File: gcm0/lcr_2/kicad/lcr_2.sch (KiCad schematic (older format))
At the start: 131 parts, among them J1 5V, J2 -5V, J3 Conn_01x01_Male, J4 Conn_01x03_Male, J5 Conn_01x01_Male, J6 Conn_01x01_Male, J8 SWD, Q1 BC547, Q2 BC547, Q3 BC547, SW1 1, SW2 2, U1 RC4580, U10 RC4580, U11 74HC595, U12 STM32F030F4P6, U2 74HC4053PW,112, U3 74HC4052PW,118, U4 RC4580, U5 LM2596S-5, U6 LM7805_TO220, U7 RC4580, U8 LM1117-3.3, U9 74HC4053PW,112, Y1 8M

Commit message: 相位幅度校准程序成功
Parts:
- added R21: 100, Resistor_THT:R_Axial_DIN0204_L3.6mm_D1.6mm_P1.90mm_Vertical, symbol Device:R
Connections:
- net GND: now also R21.2
- net at C16.1, C2.1, R19.1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: now also R21.1
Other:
- moved on the sheet: R22
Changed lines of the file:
@@
 	3500 2750 4450 2750
 Connection ~ 4450 2750
-Text Label 5600 1550 0    50   ~ 0
+Text Label 6200 1100 0    50   ~ 0
 SPWM
 $Comp
@@
 L Device:R R22
 U 1 1 625D8345
-P 5300 1550
-F 0 "R22" V 5093 1550 50  0000 C CNN
-F 1 "1K" V 5184 1550 50  0000 C CNN
-F 2 "Resistor_THT:R_Axial_DIN0204_L3.6mm_D1.6mm_P1.90mm_Vertical" V 5230 1550 50  0001 C CNN
-F 3 "~" H 5300 1550 50  0001 C CNN
-	1    5300 1550
-	0    1    1    0
-$EndComp
-Wire Wire Line
-	5150 1550 5000 1550
+P 5900 1100
+F 0 "R22" V 5693 1100 50  0000 C CNN
+F 1 "1K" V 5784 1100 50  0000 C CNN
+F 2 "Resistor_THT:R_Axial_DIN0204_L3.6mm_D1.6mm_P1.90mm_Vertical" V 5830 1100 50  0001 C CNN
+F 3 "~" H 5900 1100 50  0001 C CNN
+	1    5900 1100
+	0    1    1    0
+$EndComp
 Connection ~ 5000 1550
 Wire Wire Line
-	5450 1550 5600 1550
+	6050 1100 6200 1100
 Wire Wire Line
 	3700 1550 4100 1550
@@
 	0    1    1    0
 $EndComp
+Wire Wire Line
+	5750 1100 5350 1100
+Wire Wire Line
+	5000 1100 5000 1550
+$Comp
+L Device:R R21
+U 1 1 61E47858
+P 5350 1250
+F 0 "R21" H 5420 1296 50  0000 L CNN
+F 1 "100" H 5420 1205 50  0000 L CNN
+F 2 "Resistor_THT:R_Axial_DIN0204_L3.6mm_D1.6mm_P1.90mm_Vertical" V 5280 1250 50  0001 C CNN
+F 3 "~" H 5350 1250 50  0001 C CNN
+	1    5350 1250
+	1    0    0    -1
+$EndComp
+Connection ~ 5350 1100
+Wire Wire Line
+	5350 1100 5000 1100
+$Comp
+L power:GND #PWR09
+U 1 1 61F0040F
+P 5350 1400
+F 0 "#PWR09" H 5350 1150 50  0001 C CNN
+F 1 "GND" H 5355 1227 50  0000 C CNN
+F 2 "" H 5350 1400 50  0001 C CNN
+F 3 "" H 5350 1400 50  0001 C CNN
+	1    5350 1400
+	1    0    0    -1
+$EndComp
 $EndSCHEMATC

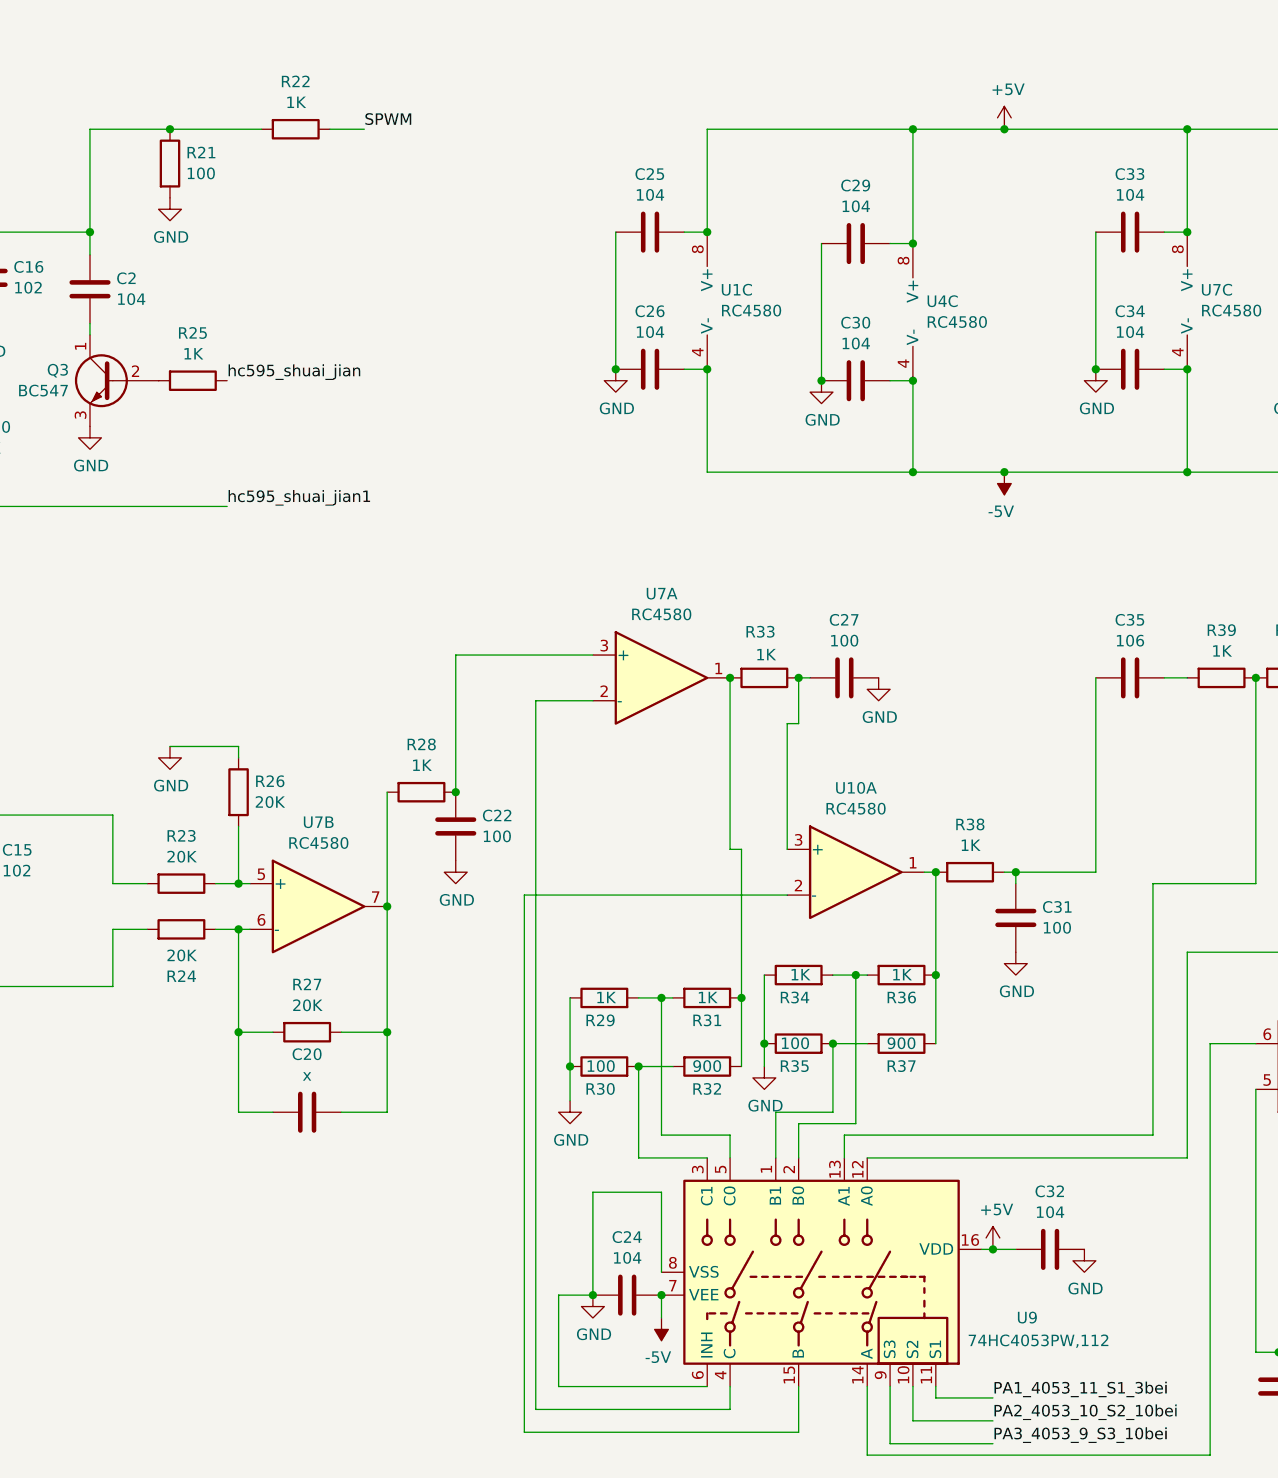
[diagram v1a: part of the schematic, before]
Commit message: 修改100KHZ的ADC触发方式
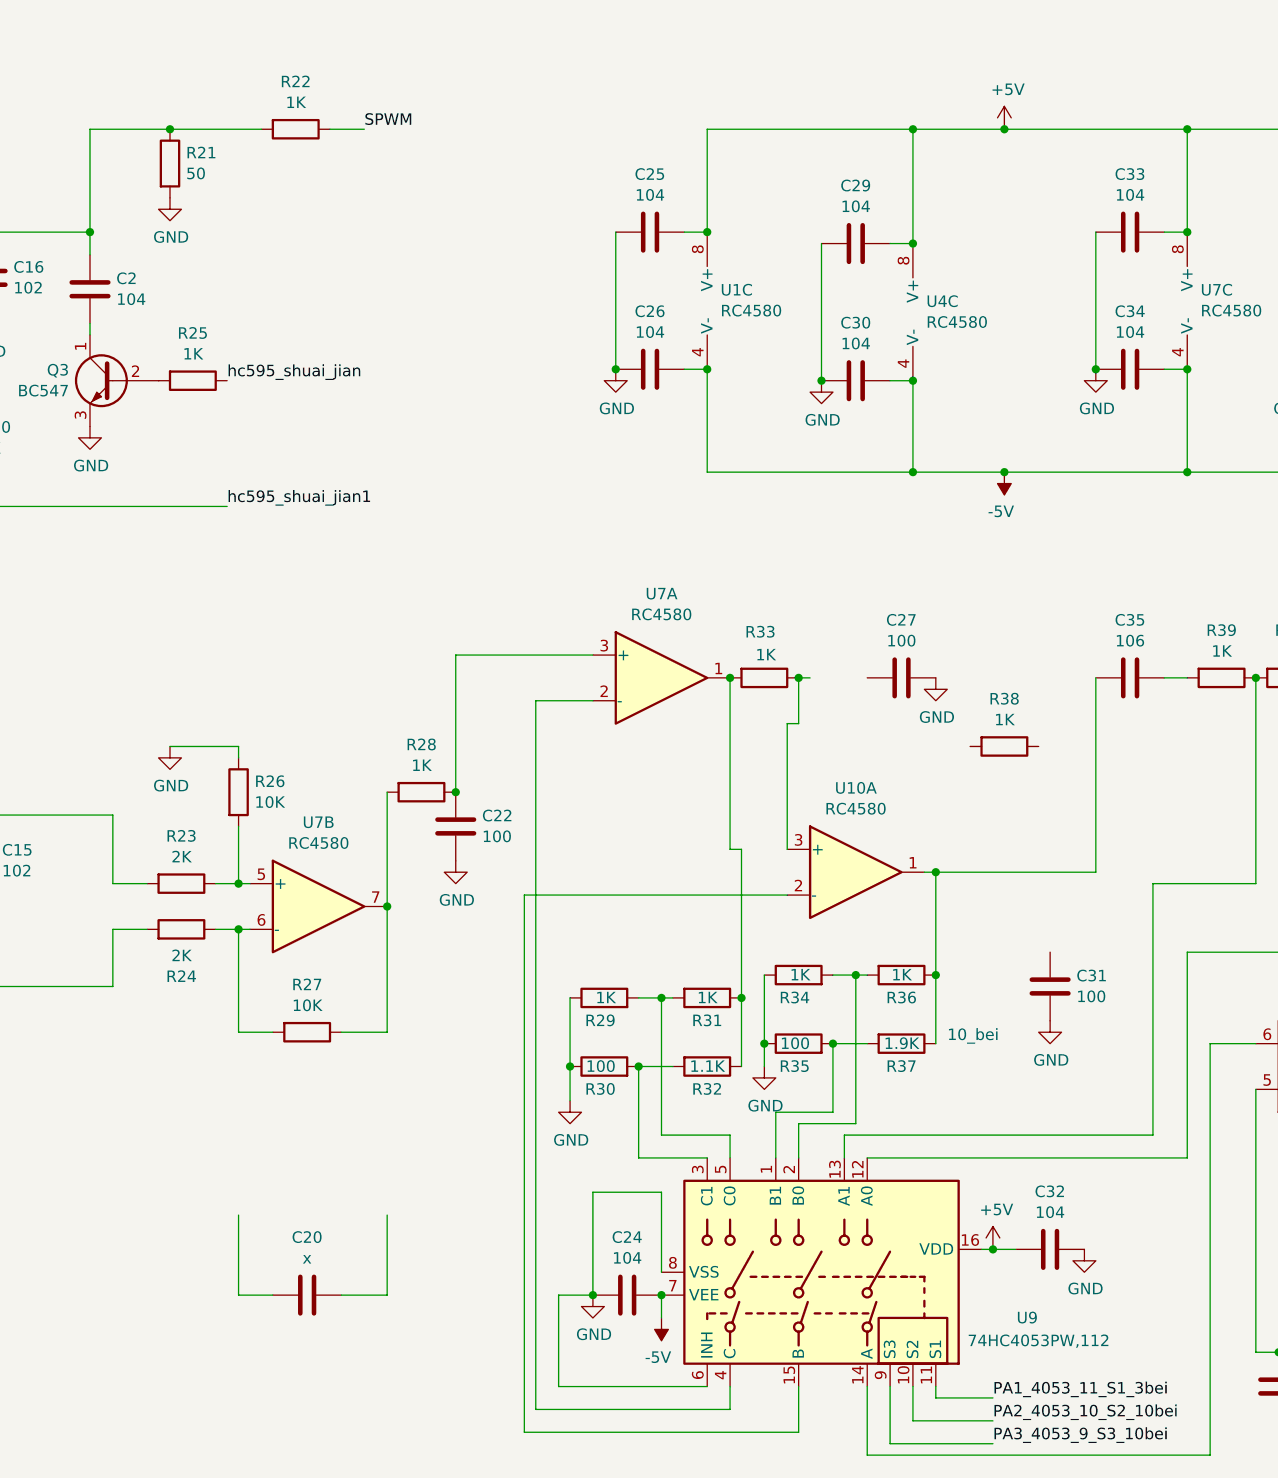
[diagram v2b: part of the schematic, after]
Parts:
- R21: value 100 -> 50
- R23, R24: value 20K -> 2K
- R26, R27: value 20K -> 10K
- R32: value 900 -> 1.1K
- R37: value 900 -> 1.9K
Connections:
- net at R24.1, R27.2, U7.6 (-): no longer C20.2
- net at R27.1, R28.2, U7.7: no longer C20.1
- net at R33.1, U10.3 (+): no longer C27.2
- net at R36.1, R37.1, U10.1: now also C35.2; no longer R38.2
- now unconnected: C31.1, R38.1
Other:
- note added: "10_bei"
- moved on the sheet: C20, C27, C31, R38
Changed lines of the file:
@@
 P 5400 4400
 F 0 "R23" V 5193 4400 50  0000 C CNN
-F 1 "20K" V 5284 4400 50  0000 C CNN
+F 1 "2K" V 5284 4400 50  0000 C CNN
 F 2 "Resistor_THT:R_Axial_DIN0204_L3.6mm_D1.6mm_P1.90mm_Vertical" V 5330 4400 50  0001 C CNN
 F 3 "~" H 5400 4400 50  0001 C CNN
@@
 P 5400 4600
 F 0 "R24" V 5193 4600 50  0000 C CNN
-F 1 "20K" V 5284 4600 50  0000 C CNN
+F 1 "2K" V 5284 4600 50  0000 C CNN
 F 2 "Resistor_THT:R_Axial_DIN0204_L3.6mm_D1.6mm_P1.90mm_Vertical" V 5330 4600 50  0001 C CNN
 F 3 "~" H 5400 4600 50  0001 C CNN
@@
 P 5650 4000
 F 0 "R26" H 5720 4046 50  0000 L CNN
-F 1 "20K" H 5720 3955 50  0000 L CNN
+F 1 "10K" H 5720 3955 50  0000 L CNN
 F 2 "Resistor_THT:R_Axial_DIN0204_L3.6mm_D1.6mm_P1.90mm_Vertical" V 5580 4000 50  0001 C CNN
 F 3 "~" H 5650 4000 50  0001 C CNN
@@
 P 5950 5050
 F 0 "R27" V 5743 5050 50  0000 C CNN
-F 1 "20K" V 5834 5050 50  0000 C CNN
+F 1 "10K" V 5834 5050 50  0000 C CNN
 F 2 "Resistor_THT:R_Axial_DIN0204_L3.6mm_D1.6mm_P1.90mm_Vertical" V 5880 5050 50  0001 C CNN
 F 3 "~" H 5950 5050 50  0001 C CNN
@@
 P 8550 5100
 F 0 "R37" V 8650 5100 50  0000 C CNN
-F 1 "900" V 8550 5100 50  0000 C CNN
+F 1 "1.9K" V 8550 5100 50  0000 C CNN
 F 2 "Resistor_THT:R_Axial_DIN0204_L3.6mm_D1.6mm_P1.90mm_Vertical" V 8480 5100 50  0001 C CNN
 F 3 "~" H 8550 5100 50  0001 C CNN
@@
 	0    1    1    0
 $EndComp
-$Comp
-L Device:C C22
-U 1 1 631C5B0A
-P 6600 4150
-F 0 "C22" H 6715 4196 50  0000 L CNN
-F 1 "100" H 6715 4105 50  0000 L CNN
-F 2 "Capacitor_SMD:C_0603_1608Metric_Pad1.08x0.95mm_HandSolder" H 6638 4000 50  0001 C CNN
-F 3 "~" H 6600 4150 50  0001 C CNN
-	1    6600 4150
-	1    0    0    -1
-$EndComp
-$Comp
-L power:GND #PWR035
-U 1 1 631C7937
-P 6600 4300
-F 0 "#PWR035" H 6600 4050 50  0001 C CNN
-F 1 "GND" H 6605 4127 50  0000 C CNN
-F 2 "" H 6600 4300 50  0001 C CNN
-F 3 "" H 6600 4300 50  0001 C CNN
-	1    6600 4300
-	1    0    0    -1
-$EndComp
 Wire Wire Line
 	7200 3400 6600 3400
@@
 Wire Wire Line
 	6600 3400 6600 4000
-Connection ~ 6600 4000
 $Comp
 L Device:C C27
 U 1 1 632A707B
-P 8300 3500
-F 0 "C27" V 8048 3500 50  0000 C CNN
-F 1 "100" V 8139 3500 50  0000 C CNN
-F 2 "Capacitor_SMD:C_0603_1608Metric_Pad1.08x0.95mm_HandSolder" H 8338 3350 50  0001 C CNN
-F 3 "~" H 8300 3500 50  0001 C CNN
-	1    8300 3500
+P 8550 3500
+F 0 "C27" V 8298 3500 50  0000 C CNN
+F 1 "100" V 8389 3500 50  0000 C CNN
+F 2 "Capacitor_SMD:C_0603_1608Metric_Pad1.08x0.95mm_HandSolder" H 8588 3350 50  0001 C CNN
+F 3 "~" H 8550 3500 50  0001 C CNN
+	1    8550 3500
 	0    1    1    0
 $EndComp
@@
 L power:GND #PWR039
 U 1 1 632AA5CA
-P 8450 3500
-F 0 "#PWR039" H 8450 3250 50  0001 C CNN
-F 1 "GND" H 8455 3327 50  0000 C CNN
-F 2 "" H 8450 3500 50  0001 C CNN
-F 3 "" H 8450 3500 50  0001 C CNN
-	1    8450 3500
+P 8700 3500
+F 0 "#PWR039" H 8700 3250 50  0001 C CNN
+F 1 "GND" H 8705 3327 50  0000 C CNN
+F 2 "" H 8700 3500 50  0001 C CNN
+F 3 "" H 8700 3500 50  0001 C CNN
+	1    8700 3500
 	1    0    0    -1
 $EndComp
@@
 Wire Wire Line
 	10100 3500 10100 4400
-$Comp
-L Device:R R38
-U 1 1 63573DB8
-P 8850 4350
-F 0 "R38" V 8643 4350 50  0000 C CNN
-F 1 "1K" V 8734 4350 50  0000 C CNN
-F 2 "Resistor_THT:R_Axial_DIN0204_L3.6mm_D1.6mm_P1.90mm_Vertical" V 8780 4350 50  0001 C CNN
-F 3 "~" H 8850 4350 50  0001 C CNN
-	1    8850 4350
-	0    1    1    0
-$EndComp
-$Comp
-L Device:C C31
-U 1 1 63575BE7
-P 9050 4550
-F 0 "C31" H 9165 4596 50  0000 L CNN
-F 1 "100" H 9165 4505 50  0000 L CNN
-F 2 "Capacitor_SMD:C_0603_1608Metric_Pad1.08x0.95mm_HandSolder" H 9088 4400 50  0001 C CNN
-F 3 "~" H 9050 4550 50  0001 C CNN
-	1    9050 4550
-	1    0    0    -1
-$EndComp
-$Comp
-L power:GND #PWR049
-U 1 1 6357784C
-P 9050 4700
-F 0 "#PWR049" H 9050 4450 50  0001 C CNN
-F 1 "GND" H 9055 4527 50  0000 C CNN
-F 2 "" H 9050 4700 50  0001 C CNN
-F 3 "" H 9050 4700 50  0001 C CNN
-	1    9050 4700
-	1    0    0    -1
-$EndComp
-Wire Wire Line
-	9000 4350 9050 4350
 Wire Wire Line
 	9400 4350 9400 3500
-Wire Wire Line
-	9050 4400 9050 4350
-Connection ~ 9050 4350
-Wire Wire Line
-	9050 4350 9400 4350
 $Comp
 L Switch:SW_Push SW1
@@
 Wire Wire Line
 	8700 4800 8700 4350
-Connection ~ 8700 4350
 Wire Wire Line
 	8700 5100 8700 4800
@@
 P 7700 5200
 F 0 "R32" V 7800 5200 50  0000 C CNN
-F 1 "900" V 7700 5200 50  0000 C CNN
+F 1 "1.1K" V 7700 5200 50  0000 C CNN
 F 2 "Resistor_THT:R_Axial_DIN0204_L3.6mm_D1.6mm_P1.90mm_Vertical" V 7630 5200 50  0001 C CNN
 F 3 "~" H 7700 5200 50  0001 C CNN
@@
 	0    1    1    0
 $EndComp
-Connection ~ 5650 5050
-Wire Wire Line
-	5650 5400 5650 5050
-Wire Wire Line
-	5800 5400 5650 5400
-Connection ~ 6300 5050
-Wire Wire Line
-	6300 5400 6300 5050
-Wire Wire Line
-	6100 5400 6300 5400
-$Comp
-L Device:C C20
-U 1 1 620378E4
-P 5950 5400
-F 0 "C20" V 5698 5400 50  0000 C CNN
-F 1 "x" V 5789 5400 50  0000 C CNN
-F 2 "Capacitor_SMD:C_0603_1608Metric_Pad1.08x0.95mm_HandSolder" H 5988 5250 50  0001 C CNN
-F 3 "~" H 5950 5400 50  0001 C CNN
-	1    5950 5400
-	0    1    1    0
-$EndComp
 Wire Wire Line
 	5750 1100 5350 1100
@@
 P 5350 1250
 F 0 "R21" H 5420 1296 50  0000 L CNN
-F 1 "100" H 5420 1205 50  0000 L CNN
+F 1 "50" H 5420 1205 50  0000 L CNN
 F 2 "Resistor_THT:R_Axial_DIN0204_L3.6mm_D1.6mm_P1.90mm_Vertical" V 5280 1250 50  0001 C CNN
 F 3 "~" H 5350 1250 50  0001 C CNN
@@
 	1    0    0    -1
 $EndComp
+$Comp
+L power:GND #PWR035
+U 1 1 631C7937
+P 6600 4300
+F 0 "#PWR035" H 6600 4050 50  0001 C CNN
+F 1 "GND" H 6605 4127 50  0000 C CNN
+F 2 "" H 6600 4300 50  0001 C CNN
+F 3 "" H 6600 4300 50  0001 C CNN
+	1    6600 4300
+	1    0    0    -1
+$EndComp
+$Comp
+L Device:C C22
+U 1 1 631C5B0A
+P 6600 4150
+F 0 "C22" H 6715 4196 50  0000 L CNN
+F 1 "100" H 6715 4105 50  0000 L CNN
+F 2 "Capacitor_SMD:C_0603_1608Metric_Pad1.08x0.95mm_HandSolder" H 6638 4000 50  0001 C CNN
+F 3 "~" H 6600 4150 50  0001 C CNN
+	1    6600 4150
+	1    0    0    -1
+$EndComp
+Wire Wire Line
+	5650 6200 5650 5850
+Wire Wire Line
+	5800 6200 5650 6200
+Wire Wire Line
+	6300 6200 6300 5850
+Wire Wire Line
+	6100 6200 6300 6200
+$Comp
+L Device:C C20
+U 1 1 620378E4
+P 5950 6200
+F 0 "C20" V 5698 6200 50  0000 C CNN
+F 1 "x" V 5789 6200 50  0000 C CNN
+F 2 "Capacitor_SMD:C_0603_1608Metric_Pad1.08x0.95mm_HandSolder" H 5988 6050 50  0001 C CNN
+F 3 "~" H 5950 6200 50  0001 C CNN
+	1    5950 6200
+	0    1    1    0
+$EndComp
+$Comp
+L power:GND #PWR049
+U 1 1 6357784C
+P 9200 5000
+F 0 "#PWR049" H 9200 4750 50  0001 C CNN
+F 1 "GND" H 9205 4827 50  0000 C CNN
+F 2 "" H 9200 5000 50  0001 C CNN
+F 3 "" H 9200 5000 50  0001 C CNN
+	1    9200 5000
+	1    0    0    -1
+$EndComp
+$Comp
+L Device:C C31
+U 1 1 63575BE7
+P 9200 4850
+F 0 "C31" H 9315 4896 50  0000 L CNN
+F 1 "100" H 9315 4805 50  0000 L CNN
+F 2 "Capacitor_SMD:C_0603_1608Metric_Pad1.08x0.95mm_HandSolder" H 9238 4700 50  0001 C CNN
+F 3 "~" H 9200 4850 50  0001 C CNN
+	1    9200 4850
+	1    0    0    -1
+$EndComp
+$Comp
+L Device:R R38
+U 1 1 63573DB8
+P 9000 3800
+F 0 "R38" V 8793 3800 50  0000 C CNN
+F 1 "1K" V 8884 3800 50  0000 C CNN
+F 2 "Resistor_THT:R_Axial_DIN0204_L3.6mm_D1.6mm_P1.90mm_Vertical" V 8930 3800 50  0001 C CNN
+F 3 "~" H 9000 3800 50  0001 C CNN
+	1    9000 3800
+	0    1    1    0
+$EndComp
+Wire Wire Line
+	9400 4350 8700 4350
+Connection ~ 8700 4350
+Text Notes 8750 5100 0    50   ~ 0
+10_bei
+Connection ~ 6600 4000
 $EndSCHEMATC

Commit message: 档位设置
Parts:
- removed R29, R31, R34, R36: 1K, Resistor_THT:R_Axial_DIN0204_L3.6mm_D1.6mm_P1.90mm_Vertical, symbol Device:R
- R1: value 100 -> 50
- R21: value 50 -> 100
- R23, R24: value 2K -> 1K
- R32: value 1.1K -> 900
- R37: value 1.9K -> 500
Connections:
- net GND: now also R35.2; no longer C31.2, R35.1
- net at R32.1, U7.1: now also U10.3 (+), U9.5 (C0); no longer R33.2
- net at U9.2 (B0): now also C35.2, R37.2, U10.1
- net at R33.1: no longer U10.3 (+)
- net PA2_4053_10_S2_10bei renamed PA2_4053_10_S2_6bei
- new net: R35.1, R37.1, U9.1 (B1)
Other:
- note added: "3_bei"
- note removed: "10_bei"
- moved on the sheet: C20, C27, C31, R33, R35, R37, R38
